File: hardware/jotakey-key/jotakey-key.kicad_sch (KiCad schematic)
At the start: 0 parts

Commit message: hardware: draw the schematic
STM32L432KCU6 with crystal-less USB through a USBLC6-2SC6 to the USB-A
edge contacts; XC6206 3.3 V LDO; OPTIGA Trust M on I2C1 (PA9/PA10)
with 4.7 kOhm pull-ups and reset on PB0; capacitive touch electrode on
TSC group 2 (PB5 through 1 kOhm, sampling capacitor on PB4); red LED on
PA8; BOOT0 pulled down; NRST, SWDIO, SWCLK, 3V3 and GND on test pads.
Every BOM part carries its LCSC and MPN fields.

KiCad 10 ERC passes except for two expected warnings: the footprint
library for the edge contacts and the touch pad comes in the next step.
jotakey-key-schematic.pdf is the same sheet exported by kicad-cli.

Co-Authored-By: Claude Opus 5.5 <noreply@anthropic.com>
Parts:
- added C1, C2, C7: 1uF, Capacitor_SMD:C_0402_1005Metric, symbol jotakey:C
- added C10: 10nF C0G, Capacitor_SMD:C_0402_1005Metric, symbol jotakey:C
- added C3: 4.7uF, Capacitor_SMD:C_0603_1608Metric, symbol jotakey:C
- added C4, C5, C6, C8, C9: 100nF, Capacitor_SMD:C_0402_1005Metric, symbol jotakey:C
- added D1: LED red, LED_SMD:LED_0603_1608Metric, symbol jotakey:LED
- added E1: TouchPad, jotakey:TouchPad_D10mm, symbol jotakey:TouchElectrode
- added J1: USB_A_PCB_Edge, jotakey:USB_A_PCB_Edge_2.0mm, symbol jotakey:USB_A_PCB_Edge
- added R1, R2: 1k, Resistor_SMD:R_0402_1005Metric, symbol jotakey:R
- added R3, R4: 4.7k, Resistor_SMD:R_0402_1005Metric, symbol jotakey:R
- added R5: 10k, Resistor_SMD:R_0402_1005Metric, symbol jotakey:R
- added TP1: SWDIO, TestPoint:TestPoint_Pad_D1.0mm, symbol jotakey:TestPoint
- added TP2: SWCLK, TestPoint:TestPoint_Pad_D1.0mm, symbol jotakey:TestPoint
- added TP3: NRST, TestPoint:TestPoint_Pad_D1.0mm, symbol jotakey:TestPoint
- added TP4: 3V3, TestPoint:TestPoint_Pad_D1.0mm, symbol jotakey:TestPoint
- added TP5: GND, TestPoint:TestPoint_Pad_D1.0mm, symbol jotakey:TestPoint
- added U1: STM32L432KCU6, Package_DFN_QFN:QFN-32-1EP_5x5mm_P0.5mm_EP3.45x3.45mm, symbol jotakey:STM32L432KCUx
- added U2: SLS32AIA010MH, Package_SON:Microchip_USON-10-1EP_3x3mm_P0.5mm_EP1.8x2.5mm, symbol jotakey:OPTIGA_Trust_M_USON10
- added U3: XC6206P332MR, Package_TO_SOT_SMD:SOT-23-3, symbol jotakey:XC6206PxxxMR
- added U4: USBLC6-2SC6, Package_TO_SOT_SMD:SOT-23-6, symbol jotakey:USBLC6-2SC6
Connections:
- new net: E1.1, R2.1
- new net: D1.2 (A), R1.2
- new net +3V3: C2.1, C3.1, C4.1, C5.1, C6.1, C7.1, C9.1, R3.1, R4.1, TP4.1, U1.1 (VDD), U1.17 (VDD), U1.5 (VDDA), U2.10 (VCC), U3.2 (VO)
- new net BOOT0: R5.1, U1.31 (PH3)
- new net GND: C1.2, C10.2, C2.2, C3.2, C4.2, C5.2, C6.2, C7.2, C8.2, C9.2, D1.1 (K), J1.4 (GND), R5.2, TP5.1, U1.16 (VSS), U1.32 (VSS), U1.33 (VSS), U2.1 (GND), U2.11 (EP), U3.1 (GND), U4.2 (GND)
- new net I2C_SCL: R4.2, U1.19 (PA9), U2.8 (SCL)
- new net I2C_SDA: R3.2, U1.20 (PA10), U2.3 (SDA)
- new net LED: R1.1, U1.18 (PA8)
- new net NRST: C8.1, TP3.1, U1.4 (NRST)
- new net SE_RST: U1.14 (PB0), U2.9 (~{RST})
- new net SWCLK: TP2.1, U1.24 (PA14)
- new net SWDIO: TP1.1, U1.23 (PA13)
- new net TOUCH_CS: C10.1, U1.27 (PB4)
- new net TOUCH_SENSE: R2.2, U1.28 (PB5)
- new net USB_CONN_DM: J1.2 (D-), U4.1 (I/O1)
- new net USB_CONN_DP: J1.3 (D+), U4.3 (I/O2)
- new net USB_DM: U1.21 (PA11), U4.6 (I/O1)
- new net USB_DP: U1.22 (PA12), U4.4 (I/O2)
- new net VBUS: C1.1, J1.1 (VBUS), U3.3 (VI), U4.5 (VBUS)
- no-connect marks 0 -> 15
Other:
- company: (none) -> Jotakey
- title: (none) -> Jotakey key: STM32L432 + OPTIGA Trust M USB-A dongle

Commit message: hardware: add the board's footprints
USB_A_PCB_Edge_2.0mm follows the USB 2.0 Series A plug drawing (spec
Fig. 6-9): contacts at +-1.0 and +-3.5 mm, pads 1.5 mm wide, VBUS/GND
starting 1.0 mm from the edge and D-/D+ 2.0 mm so power mates first,
no paste, excluded from BOM and placement. TouchPad_D10mm is a 10 mm
electrode under solder mask. The OPTIGA gets a copy of KiCad's USON-10
with the exposed pad narrowed from 1.8 to Infineon's 1.7 mm; the
STM32's stock QFN-32 already matches ST's recommended land pattern.

The footprint library is registered in fp-lib-table and ERC now
reports no violations. KiCad filled in the project file's defaults.

Co-Authored-By: Claude Opus 5.5 <noreply@anthropic.com>
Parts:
- U2: footprint Package_SON:Microchip_USON-10-1EP_3x3mm_P0.5mm_EP1.8x2.5mm -> jotakey:Infineon_PG-USON-10-2_3x3mm_P0.5mm_EP1.7x2.5mm
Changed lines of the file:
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@@
 			)
 		)
-		(property "Footprint" "Package_SON:Microchip_USON-10-1EP_3x3mm_P0.5mm_EP1.8x2.5mm"
+		(property "Footprint" "jotakey:Infineon_PG-USON-10-2_3x3mm_P0.5mm_EP1.7x2.5mm"
 			(at 248.92 101.6 0)
 			(hide yes)

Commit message: hardware: name the touch electrode net, centre U4 and swap its channels
The touch electrode's net gets a label, TOUCH_ELECTRODE, instead of
KiCad's generated Net-(E1-~).

U4 (USBLC6-2SC6) moves onto the board's centre line. Its two channels
are identical, so D- now passes through pins 3/4 and D+ through pins 1/6.
This puts the one unavoidable D+/D- crossing between U4 and the MCU,
where there is room for vias, instead of on the USB-A tongue.

Co-Authored-By: Claude Opus 5.5 <noreply@anthropic.com>
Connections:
- net USB_CONN_DM: now also U4.3 (I/O2); no longer U4.1 (I/O1)
- net USB_CONN_DP: now also U4.1 (I/O1); no longer U4.3 (I/O2)
- net USB_DM: now also U4.4 (I/O2); no longer U4.6 (I/O1)
- net USB_DP: now also U4.6 (I/O1); no longer U4.4 (I/O2)
- net TOUCH_ELECTRODE: now reaches E1.1, R2.1
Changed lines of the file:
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@@
 		(pts
 			(xy 45.72 49.53)
-			(xy 57.15 49.53)
-		)
-	)
-	(wire
-		(pts
-			(xy 57.15 49.53)
-			(xy 57.15 50.8)
-		)
-	)
-	(wire
-		(pts
-			(xy 57.15 50.8)
+			(xy 46.99 49.53)
+		)
+	)
+	(wire
+		(pts
+			(xy 62.23 50.8)
 			(xy 68.58 50.8)
 		)
@@
 		(pts
 			(xy 45.72 52.07)
-			(xy 59.69 52.07)
-		)
-	)
-	(wire
-		(pts
-			(xy 59.69 52.07)
-			(xy 59.69 53.34)
-		)
-	)
-	(wire
-		(pts
-			(xy 59.69 53.34)
+			(xy 46.99 52.07)
+		)
+	)
+	(wire
+		(pts
+			(xy 62.23 53.34)
 			(xy 68.58 53.34)
 		)
@@
 		)
 	)
-	(label "USB_DM"
+	(label "USB_DP"
 		(at 81.28 50.8 0)
 		(effects
@@
 		)
 	)
-	(label "USB_DP"
+	(label "USB_DM"
 		(at 81.28 53.34 0)
 		(effects
@@
 		)
 	)
+	(label "TOUCH_ELECTRODE"
+		(at 95.25 132.08 0)
+		(effects
+			(font
+				(size 1.27 1.27)
+			)
+			(justify left bottom)
+		)
+	)
 	(label "LED"
 		(at 175.26 101.6 0)
@@
 		(effects
 			(font
+				(size 1.27 1.27)
+			)
+			(justify left bottom)
+		)
+	)
+	(label "USB_CONN_DP"
+		(at 62.23 50.8 0)
+		(effects
+			(font
+				(size 1.27 1.27)
+			)
+			(justify left bottom)
+		)
+	)
+	(label "USB_CONN_DM"
+		(at 62.23 53.34 0)
+		(effects
+			(font

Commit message: hardware: route the board
tools/route.py routes the board from the placement: keep-outs (nothing
under the touch electrode, a 1 mm ground gap around it, no vias or
bottom copper on the USB-A tongue, 0.5 mm from the board edge), the
critical nets by hand (USB with its one D+/D- crossing, VBUS, the touch
electrode trace, the capacitors and NRST under the MCU), Freerouting 2.5
for the rest, then GND pours on both layers. DRC: no errors and no
unconnected items.

To make the board routable:
- the LED moves from PA8 (pin 18) to PA3 (pin 9), off the crowded top
  row of the MCU and next to the LED;
- the OPTIGA reset moves from PB0 (pin 14) to PA5 (pin 11);
- the OPTIGA moves to the top-right corner, rotated so SCL, RST and VCC
  face the MCU; its pull-ups and decoupling move with it;
- R1 turns round so the LED track does not wrap around it.
HARDWARE.md records the new pins.

tools/silk.py moves reference designators to the fab layers (they cannot
sit beside 0402 parts on this board without covering pads) and marks a
2 x 10 mm block on the bottom silkscreen for JLCPCB's serial number.

Co-Authored-By: Claude Opus 5.5 <noreply@anthropic.com>
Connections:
- net LED: now also U1.9 (PA3); no longer U1.18 (PA8)
- net SE_RST: now also U1.11 (PA5); no longer U1.14 (PB0)
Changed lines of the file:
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@@
 	)
 	(no_connect
-		(at 172.72 88.9)
+		(at 172.72 101.6)
 	)
 	(no_connect
@@
 	)
 	(no_connect
-		(at 172.72 93.98)
+		(at 147.32 99.06)
 	)
 	(no_connect
@@
 	(wire
 		(pts
-			(xy 147.32 99.06)
-			(xy 144.78 99.06)
+			(xy 172.72 93.98)
+			(xy 175.26 93.98)
 		)
 	)
@@
 	(wire
 		(pts
-			(xy 172.72 101.6)
-			(xy 175.26 101.6)
+			(xy 172.72 88.9)
+			(xy 175.26 88.9)
 		)
 	)
@@
 	)
 	(label "SE_RST"
-		(at 144.78 99.06 180)
-		(effects
-			(font
-				(size 1.27 1.27)
-			)
-			(justify right bottom)
+		(at 175.26 93.98 0)
+		(effects
+			(font
+				(size 1.27 1.27)
+			)
+			(justify left bottom)
 		)
 	)
@@
 	)
 	(label "LED"
-		(at 175.26 101.6 0)
-		(effects
-			(font
+		(at 175.26 88.9 0)
+		(effects
+			(font

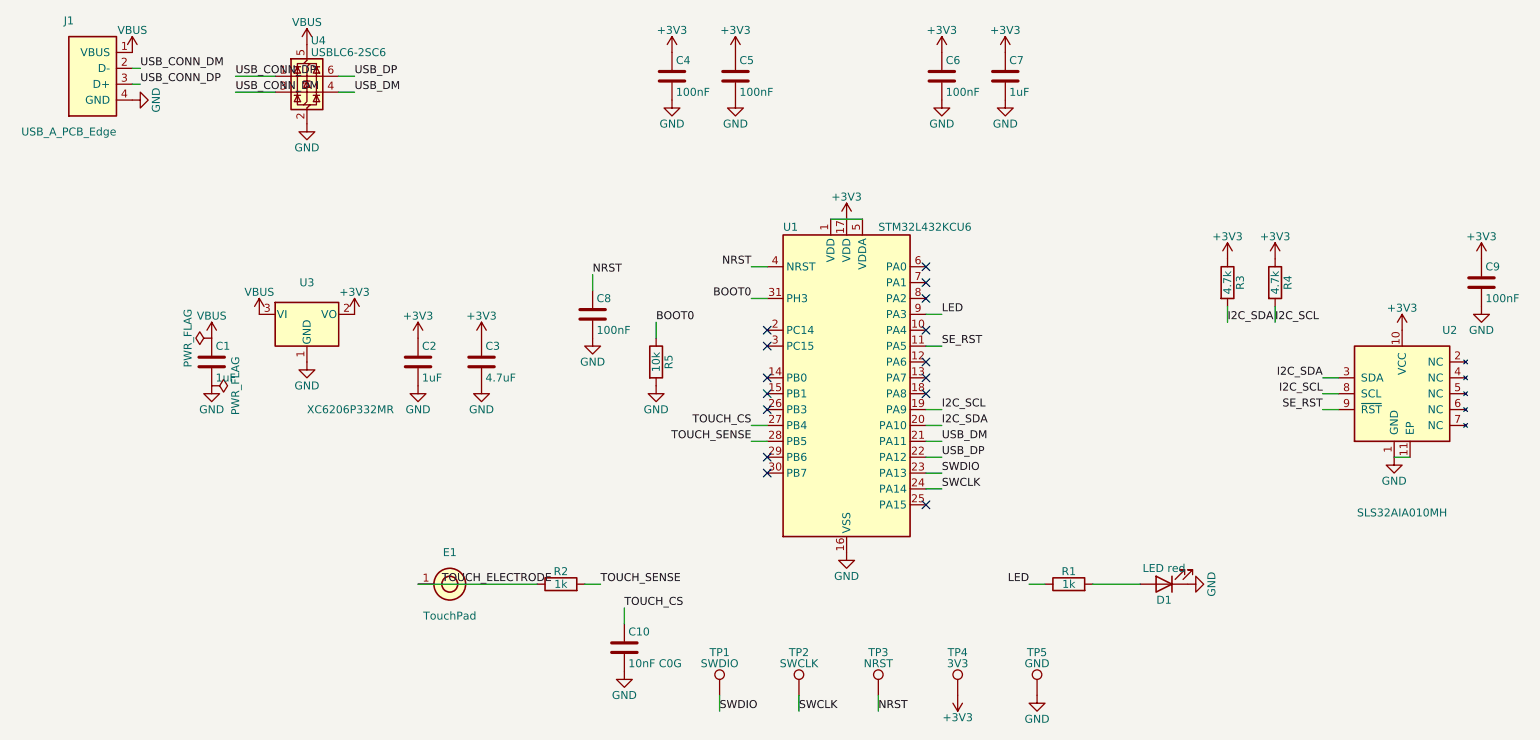
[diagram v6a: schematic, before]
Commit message: hw: 0R bring-up links R6, R7; hardware 0.2.0
Split the 3.3 V supply into +3V3 (LDO), +3V3_MCU (via R6) and
+3V3_SE (via R7) so a hand-built board can be brought up one stage at
a time. The I2C pull-ups move to the OPTIGA's rail so they cannot
back-power it while R7 is open.

Board: R6 between the LDO and U4, R7 beside U4, R3 0.4 mm right, the
SE rail over U2 and down the edge to C9, a GND via to stitch the top
pour. ERC, DRC and schematic parity clean. HARDWARE.md, MANUFACTURING.md
(staged bring-up), README, chapter 7, renders and PDFs updated.

Co-Authored-By: Claude Opus 5.5 <noreply@anthropic.com>
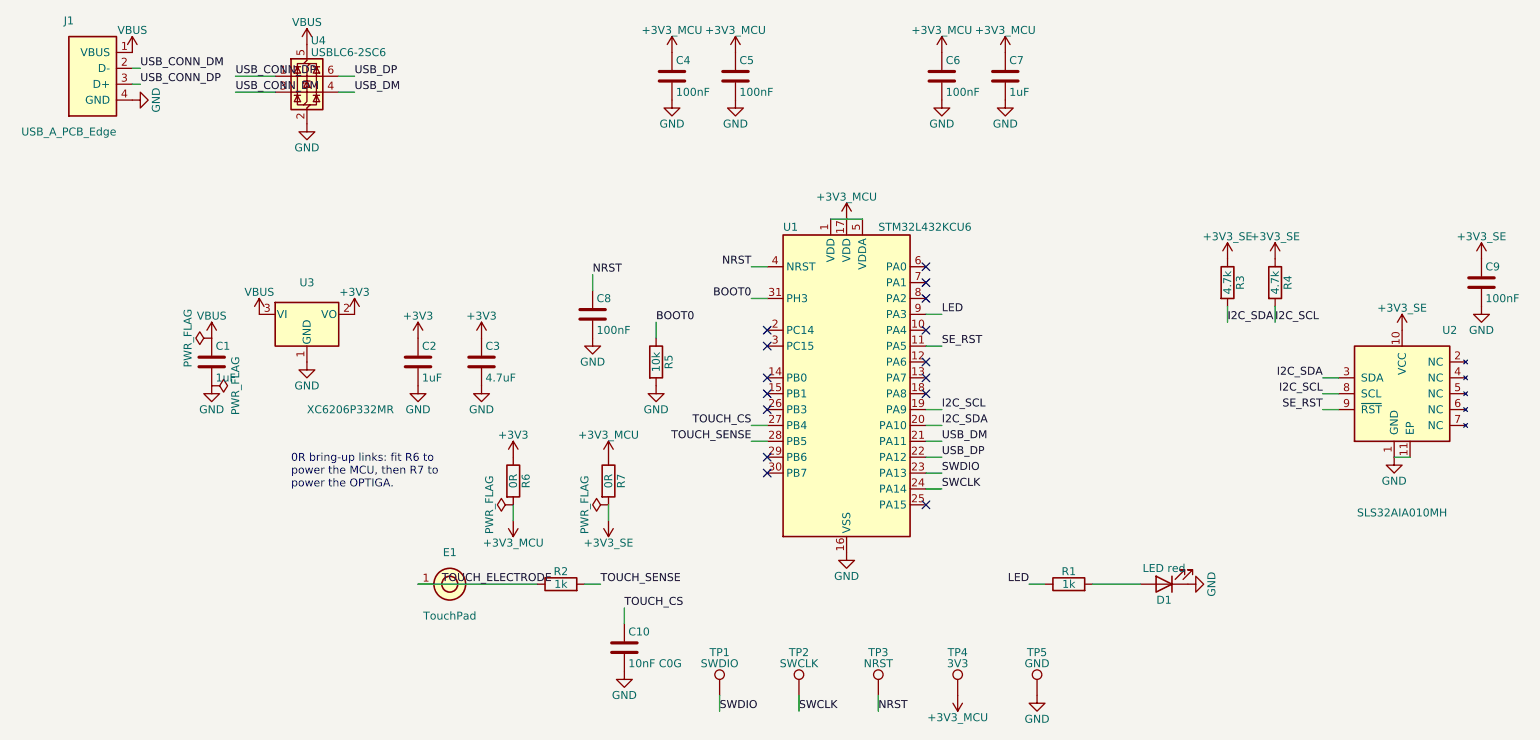
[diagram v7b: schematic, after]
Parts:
- added R6, R7: 0R, Resistor_SMD:R_0402_1005Metric, symbol jotakey:R
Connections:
- net +3V3: now also R6.1; no longer C4.1, C5.1, C6.1, C7.1, C9.1, R3.1, R4.1, TP4.1, U1.1 (VDD), U1.17 (VDD), U1.5 (VDDA), U2.10 (VCC)
- new net +3V3_MCU: C4.1, C5.1, C6.1, C7.1, R6.2, R7.1, TP4.1, U1.1 (VDD), U1.17 (VDD), U1.5 (VDDA)
- new net +3V3_SE: C9.1, R3.1, R4.1, R7.2, U2.10 (VCC)
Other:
- note added: "0R bring-up links: fit R6 to power the MCU, then R7 to power the OPTIGA."
